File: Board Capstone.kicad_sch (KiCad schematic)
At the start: 14 parts, among them J101 Power, J102 Conn_JetsonNano, J103 Status_LED, J104 Warning_LED, J105 Lidar Power, SW101 SW_Pairing, U101 SN74LV1T125DBV, U102 SN74LV1T125DBV

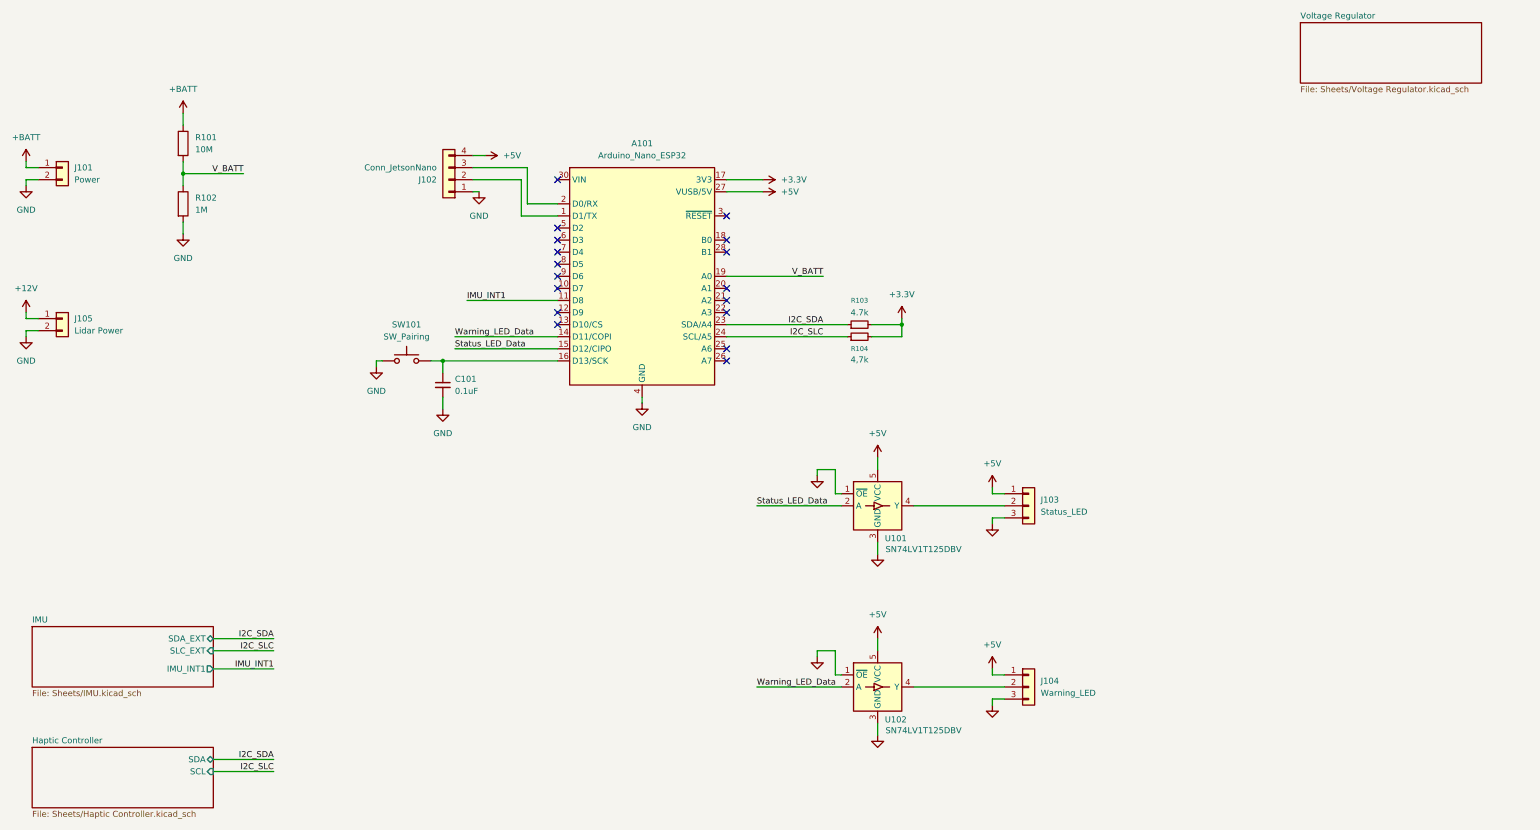
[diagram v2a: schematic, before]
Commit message: Rev 2.0 Remove MCU, IMU, Haptics controller. Add Jetson connector, Battery protection, ADC. Etc.
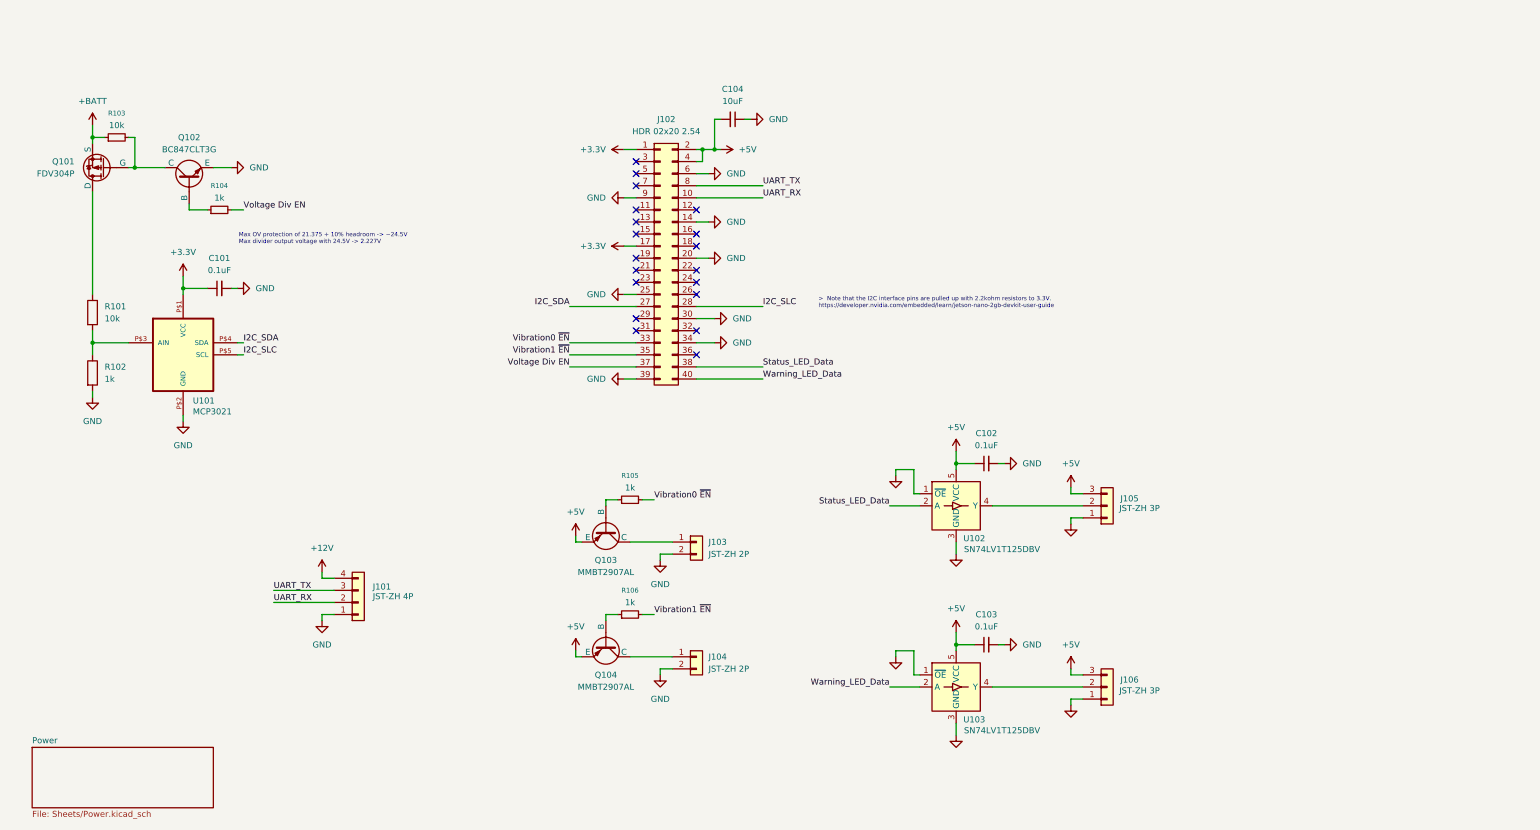
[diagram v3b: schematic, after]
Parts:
- removed A101: Arduino_Nano_ESP32, Module:Arduino_Nano, symbol MCU_Module:Arduino_Nano_ESP32
- removed J101: Power, Connector_JST:JST_XH_B2B-XH-A_1x02_P2.50mm_Vertical, symbol Connector_Generic:Conn_01x02
- removed J102: Conn_JetsonNano, Connector_JST:JST_XH_B4B-XH-A_1x04_P2.50mm_Vertical, symbol Connector_Generic:Conn_01x04
- removed J105: Lidar Power, Connector_JST:JST_XH_B2B-XH-A_1x02_P2.50mm_Vertical, symbol Connector_Generic:Conn_01x02
- removed SW101: SW_Pairing, Button_Switch_THT:SW_PUSH_6mm, symbol Switch:SW_Push
- added C102, C103: 0.1uF, Capacitor_SMD:C_1206_3216Metric_Pad1.33x1.80mm_HandSolder, symbol Device:C_Small
- added C104: 10uF, Capacitor_SMD:C_1206_3216Metric_Pad1.33x1.80mm_HandSolder, symbol Device:C_Small
- added J101: JST-ZH 4P, Connector_JST:JST_ZH_B4B-ZR_1x04_P1.50mm_Vertical, symbol Connector_Generic:Conn_01x04
- added J102: HDR 02x20 2.54, Connector_IDC:IDC-Header_2x20_P2.54mm_Horizontal, symbol Connector_Generic:Conn_02x20_Odd_Even
- added J103, J104: JST-ZH 2P, Connector_JST:JST_ZH_B2B-ZR_1x02_P1.50mm_Vertical, symbol Connector_Generic:Conn_01x02
- added Q101: FDV304P, Package_TO_SOT_SMD:SOT-23-3, symbol Simulation_SPICE:PMOS
- added Q102: BC847CLT3G, Package_TO_SOT_SMD:SOT-23, symbol Simulation_SPICE:NPN
- added Q103, Q104: MMBT2907AL, Package_TO_SOT_SMD:SOT-23, symbol Simulation_SPICE:PNP
- added R105, R106: 1k, Resistor_SMD:R_1206_3216Metric_Pad1.30x1.75mm_HandSolder, symbol Device:R_Small
- added U101: MCP3021, MCP3021:SOT-23, symbol MCP3021:MCP3021
- J105: renamed from J103; value Status_LED -> JST-ZH 3P; footprint Connector_JST:JST_ZH_B3B-ZR_1x03_P1.50mm_Vertical -> Connector_JST:JST_ZH_B2B-ZR_1x02_P1.50mm_Vertical
- J106: renamed from J104; value Warning_LED -> JST-ZH 3P
- R101: value 10M -> 10k; footprint Resistor_THT:R_Axial_DIN0207_L6.3mm_D2.5mm_P7.62mm_Horizontal -> Resistor_SMD:R_1206_3216Metric_Pad1.30x1.75mm_HandSolder
- R102: value 1M -> 1k; footprint Resistor_THT:R_Axial_DIN0207_L6.3mm_D2.5mm_P7.62mm_Horizontal -> Resistor_SMD:R_1206_3216Metric_Pad1.30x1.75mm_HandSolder
- R103: value 4.7k -> 10k
- R104: value 4,7k -> 1k
- renumbered U101 to U102, U102 to U103
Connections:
- net +12V: now also J101.4 (Pin_4)
- net +3.3V: now also C101.1, J102.1 (Pin_1), J102.17 (Pin_17), U101.P$1 (VCC); no longer R103.2, R104.2
- net +5V: now also J105.3 (Pin_3), J106.3 (Pin_3), C102.1, C103.1, C104.2, J102.2 (Pin_2), J102.4 (Pin_4), Q103.3 (E), Q104.3 (E); no longer J105.1 (Pin_1), J106.1 (Pin_1)
- net +BATT: now also R103.1, Q101.3 (S); no longer R101.1
- net GND: now also J105.1 (Pin_1), J106.1 (Pin_1), C102.2, C103.2, C104.1, J101.1 (Pin_1), J102.14 (Pin_14), J102.20 (Pin_20), J102.25 (Pin_25), J102.30 (Pin_30), J102.34 (Pin_34), J102.39 (Pin_39), J102.6 (Pin_6), J102.9 (Pin_9), J103.2 (Pin_2), J104.2 (Pin_2), Q102.3 (E), U101.P$2 (GND); no longer J105.3 (Pin_3), J106.3 (Pin_3)
- net I2C_SDA: now also J102.27 (Pin_27), U101.P$4 (SDA); no longer R103.1
- net I2C_SLC: now also J102.28 (Pin_28), U101.P$5 (SCL); no longer R104.1
- net Status_LED_Data: now also J102.38 (Pin_38)
- net Warning_LED_Data: now also J102.40 (Pin_40)
- net V_BATT: no longer names the net of R101.2, R102.1
- net V_BATT: now also U101.P$3 (AIN)
- new net: Q101.1 (D), R101.1
- new net: Q101.2 (G), Q102.1 (C), R103.2
- new net: Q104.2 (B), R106.1
- new net: J103.1 (Pin_1), Q103.1 (C)
- new net: Q103.2 (B), R105.1
- new net: Q102.2 (B), R104.1
- new net: J104.1 (Pin_1), Q104.1 (C)
- new net UART_RX: J101.2 (Pin_2), J102.10 (Pin_10)
- new net UART_TX: J101.3 (Pin_3), J102.8 (Pin_8)
- new net Vibration0 ~{EN}: J102.33 (Pin_33), R105.2
- new net Vibration1 ~{EN}: J102.35 (Pin_35), R106.2
- new net Voltage Div EN: J102.37 (Pin_37), R104.2
- no-connect marks 17 -> 19
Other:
- sheet Voltage Regulator renamed Power
- removed sheet Haptic Controller
- removed sheet IMU
- sheet Power: file Sheets/Voltage Regulator.kicad_sch -> Sheets/Power.kicad_sch
- note added: "> Note that the I2C interface pins are pulled up with 2.2kohm resistors to 3.3V. https://developer.nvidia.com/embedded/learn/jetson-nano-2gb-devkit-user-guide"
- note added: "Max OV protection of 21.375 + 10% headroom -> ~24.5V Max divider output voltage with 24.5V -> 2.227V"
- moved on the sheet: J105, J106, R101, R102, U102, U103

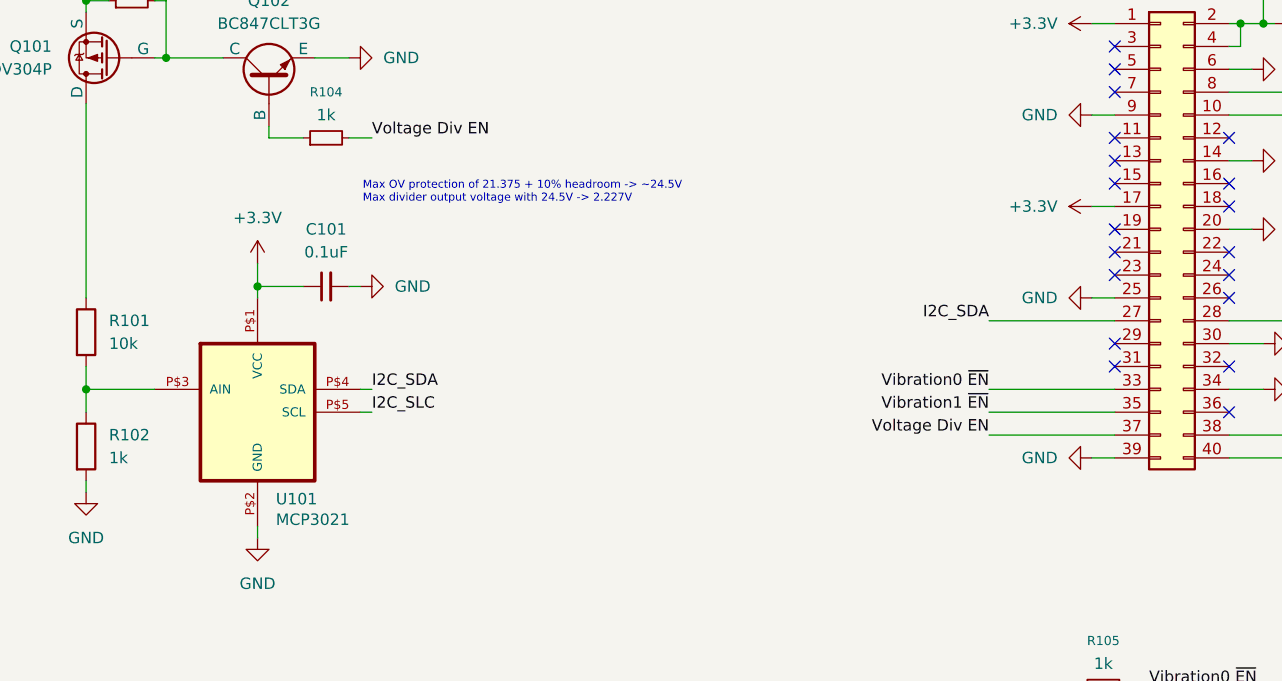
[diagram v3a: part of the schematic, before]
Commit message: Rev 2.1 Add pcb and footprint changes
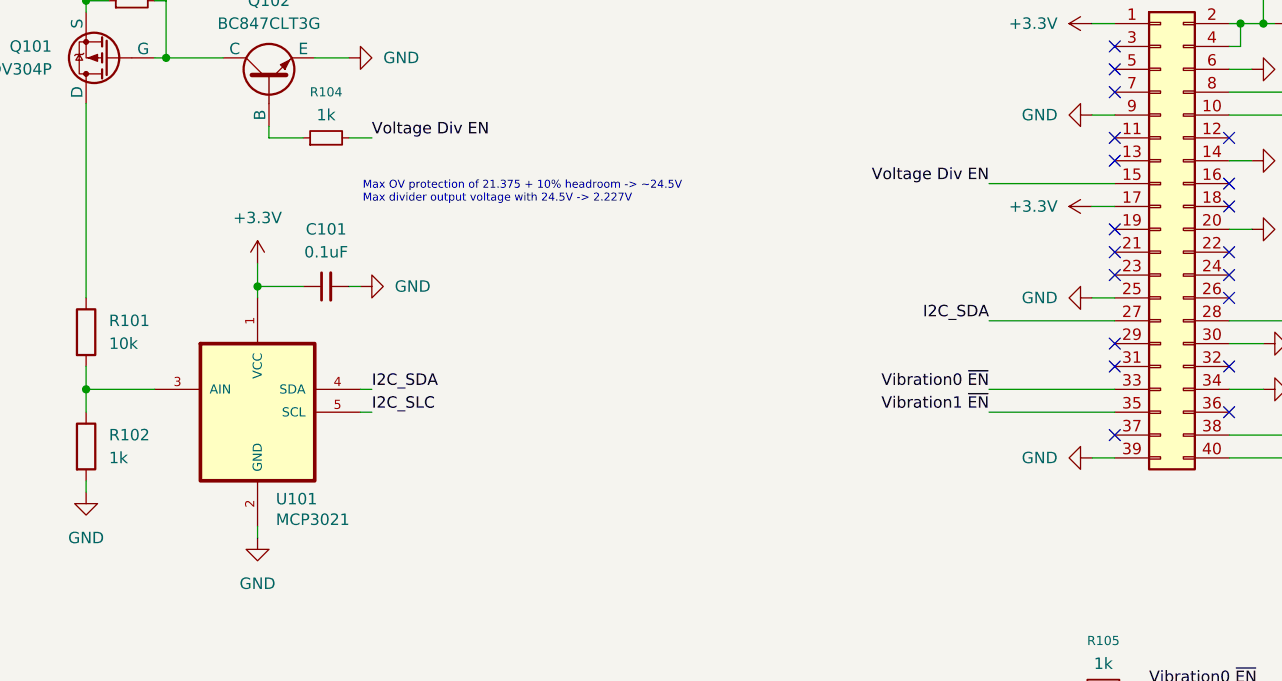
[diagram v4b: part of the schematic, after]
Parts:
- J101: footprint Connector_JST:JST_ZH_B4B-ZR_1x04_P1.50mm_Vertical -> Connector_JST:JST_ZH_S4B-ZR-SM4A-TF_1x04-1MP_P1.50mm_Horizontal
- J103, J104: footprint Connector_JST:JST_ZH_B2B-ZR_1x02_P1.50mm_Vertical -> Connector_JST:JST_ZH_S2B-ZR-SM4A-TF_1x02-1MP_P1.50mm_Horizontal
- J105: footprint Connector_JST:JST_ZH_B2B-ZR_1x02_P1.50mm_Vertical -> Connector_JST:JST_ZH_S3B-ZR-SM4A-TF_1x03-1MP_P1.50mm_Horizontal
- J106: footprint Connector_JST:JST_ZH_B3B-ZR_1x03_P1.50mm_Vertical -> Connector_JST:JST_ZH_S3B-ZR-SM4A-TF_1x03-1MP_P1.50mm_Horizontal
- U101: footprint MCP3021:SOT-23 -> Package_TO_SOT_SMD:SOT-23-5_HandSoldering
- U102, U103: footprint Package_TO_SOT_SMD:SOT-23-5 -> Package_TO_SOT_SMD:SOT-23-5_HandSoldering
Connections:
- net +3.3V: now also U101.1 (VCC); no longer U101.P$1 (VCC)
- net GND: now also U101.2 (GND); no longer U101.P$2 (GND)
- net I2C_SDA: now also U101.4 (SDA); no longer U101.P$4 (SDA)
- net I2C_SLC: now also U101.5 (SCL); no longer U101.P$5 (SCL)
- net Voltage Div EN: now also J102.15 (Pin_15); no longer J102.37 (Pin_37)
- net at R101.2, R102.1: now also U101.3 (AIN); no longer U101.P$3 (AIN)
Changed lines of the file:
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@@
 	(title_block
 		(title "Cyclops (Team 30)")
-		(date "2025-12-10")
-		(rev "2.0")
+		(date "2025-12-16")
+		(rev "2.1")
 		(company "Concordia University, Department of Electrical and Computer Engineering")
 	)
@@
 	)
 	(junction
-		(at 168.91 39.37)
+		(at 38.1 80.01)
 		(diameter 0)
 		(color 0 0 0 0)
 	)
 	(junction
-		(at 38.1 80.01)
+		(at 168.91 39.37)
 		(diameter 0)
 		(color 0 0 0 0)
@@
 	)
 	(no_connect
-		(at 152.4 57.15)
-	)
-	(no_connect
 		(at 165.1 64.77)
 	)
@@
 		(at 152.4 62.23)
 	)
+	(no_connect
+		(at 152.4 85.09)
+	)
 	(wire
 		(pts
@@
 	(wire
 		(pts
-			(xy 38.1 80.01) (xy 38.1 82.55)
-		)
-		(stroke
-			(width 0)
-			(type default)
-		)
-	)
-	(wire
-		(pts
 			(xy 138.43 72.39) (xy 152.4 72.39)
 		)
@@
 	(wire
 		(pts
+			(xy 38.1 80.01) (xy 45.72 80.01)
+		)
+		(stroke
+			(width 0)
+			(type default)
+		)
+	)
+	(wire
+		(pts
 			(xy 46.99 43.18) (xy 53.34 43.18)
 		)
@@
 	(wire
 		(pts
+			(xy 138.43 57.15) (xy 152.4 57.15)
+		)
+		(stroke
+			(width 0)
+			(type default)
+		)
+	)
+	(wire
+		(pts
 			(xy 210.82 106.68) (xy 207.01 106.68)
 		)
@@
 	(wire
 		(pts
-			(xy 138.43 85.09) (xy 152.4 85.09)
-		)
-		(stroke
-			(width 0)
-			(type default)
-		)
-	)
-	(wire
-		(pts
 			(xy 157.48 148.59) (xy 160.02 148.59)
 		)
@@
 	(wire
 		(pts
-			(xy 38.1 80.01) (xy 45.72 80.01)
+			(xy 38.1 80.01) (xy 38.1 82.55)
 		)
 		(stroke
@@
 		)
 	)
-	(label "Voltage Div EN"
-		(at 138.43 85.09 180)
+	(label "I2C_SDA"
+		(at 138.43 72.39 180)
 		(effects
 			(font
@@
 		)
 	)
-	(label "I2C_SDA"
-		(at 138.43 72.39 180)
+	(label "Voltage Div EN"
+		(at 138.43 57.15 180)
 		(effects
 			(font
@@
 			)
 		)
-		(property "Footprint" "Connector_JST:JST_ZH_B2B-ZR_1x02_P1.50mm_Vertical"
+		(property "Footprint" "Connector_JST:JST_ZH_S3B-ZR-SM4A-TF_1x03-1MP_P1.50mm_Horizontal"
 			(at 251.46 114.3 0)
 			(effects
@@
 			)
 		)
-		(property "Footprint" "Connector_JST:JST_ZH_B2B-ZR_1x02_P1.50mm_Vertical"
+		(property "Footprint" "Connector_JST:JST_ZH_S2B-ZR-SM4A-TF_1x02-1MP_P1.50mm_Horizontal"
 			(at 165.1 121.92 0)
 			(effects
@@
 			)
 		)
-		(property "Footprint" "Connector_JST:JST_ZH_B3B-ZR_1x03_P1.50mm_Vertical"
+		(property "Footprint" "Connector_JST:JST_ZH_S3B-ZR-SM4A-TF_1x03-1MP_P1.50mm_Horizontal"
 			(at 251.46 152.4 0)
 			(effects
@@
 			)
 		)
-		(property "Footprint" "Package_TO_SOT_SMD:SOT-23-5"
+		(property "Footprint" "Package_TO_SOT_SMD:SOT-23-5_HandSoldering"
 			(at 219.71 138.43 0)
 			(effects
@@
 			)
 		)
-		(property "Footprint" "Connector_JST:JST_ZH_B4B-ZR_1x04_P1.50mm_Vertical"
+		(property "Footprint" "Connector_JST:JST_ZH_S4B-ZR-SM4A-TF_1x04-1MP_P1.50mm_Horizontal"
 			(at 93.98 134.62 0)
 			(effects
@@
 			)
 		)
-		(property "Footprint" "Package_TO_SOT_SMD:SOT-23-5"
+		(property "Footprint" "Package_TO_SOT_SMD:SOT-23-5_HandSoldering"
 			(at 219.71 176.53 0)
 			(effects
@@
 			)
 		)
-		(property "Footprint" "Connector_JST:JST_ZH_B2B-ZR_1x02_P1.50mm_Vertical"
+		(property "Footprint" "Connector_JST:JST_ZH_S2B-ZR-SM4A-TF_1x02-1MP_P1.50mm_Horizontal"
 			(at 165.1 146.05 0)
 			(effects
@@
 			)
 		)
-		(property "Footprint" "MCP3021:SOT-23"
+		(property "Footprint" "Package_TO_SOT_SMD:SOT-23-5_HandSoldering"
 			(at 63.5 88.9 0)
 			(effects
@@
 			)
 		)
-		(pin "P$3"
+		(pin "3"
 		)
-		(pin "P$4"
+		(pin "4"
 		)
-		(pin "P$1"
+		(pin "5"
 		)
-		(pin "P$5"
+		(pin "2"
 		)
-		(pin "P$2"
+		(pin "1"
 		)
 		(instances

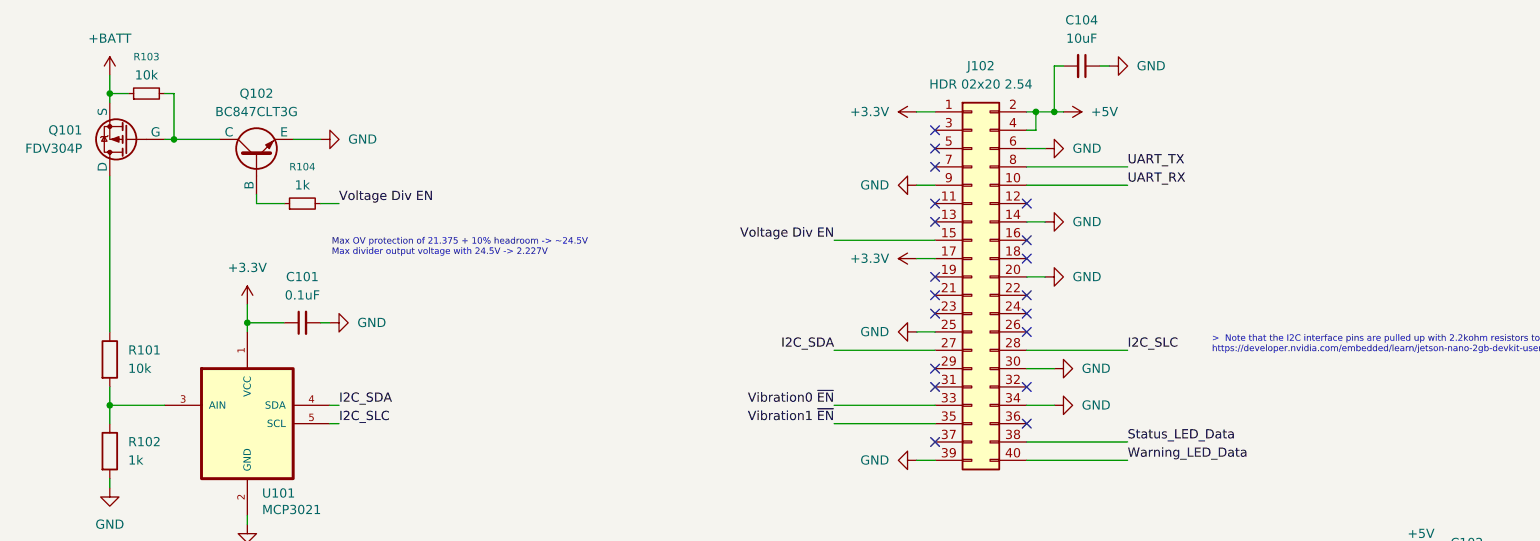
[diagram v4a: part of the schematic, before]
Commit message: Rev 2.2 Added test point and status LED
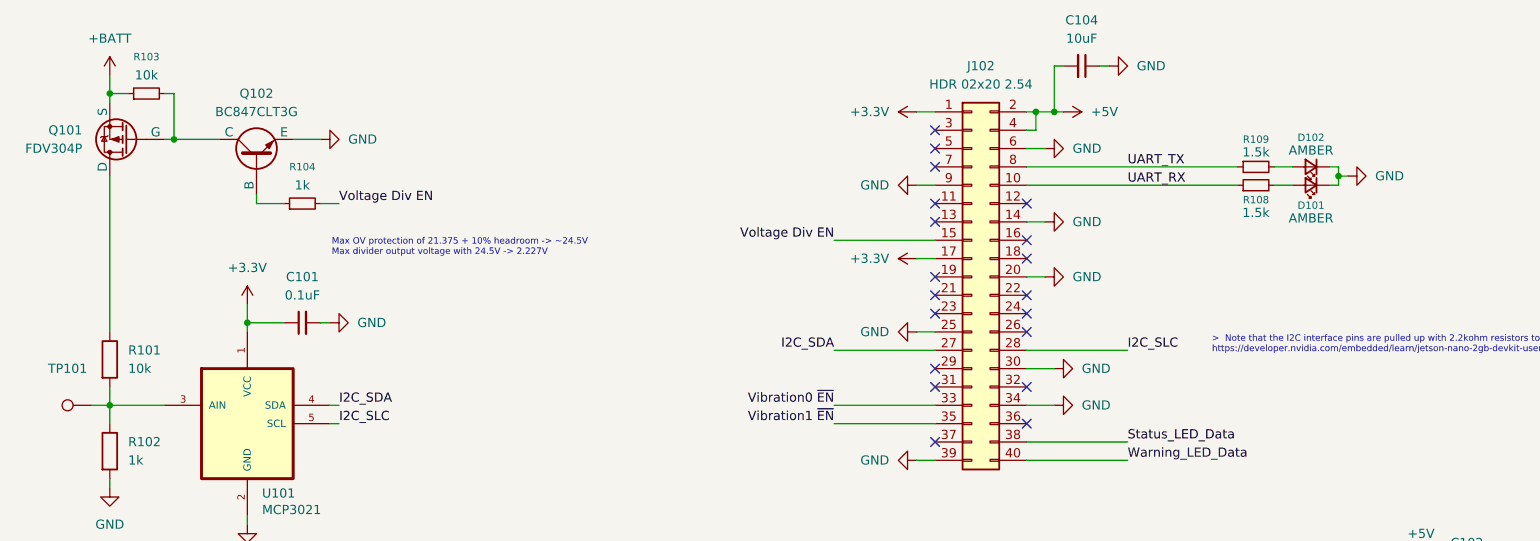
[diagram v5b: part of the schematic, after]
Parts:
- added D101, D102: AMBER, LED_SMD:LED_0603_1608Metric_Pad1.05x0.95mm_HandSolder, symbol Device:LED_Small
- added R108, R109: 1.5k, Resistor_SMD:R_1206_3216Metric_Pad1.30x1.75mm_HandSolder, symbol Device:R_Small
- added TP101: ~, TestPoint:TestPoint_Pad_D2.5mm, symbol Connector:TestPoint
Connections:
- net GND: now also D101.1 (K), D102.1 (K)
- net UART_RX: now also R108.1
- net UART_TX: now also R109.1
- net at R101.2, R102.1, U101.3 (AIN): now also TP101.1
- new net: D101.2 (A), R108.2
- new net: D102.2 (A), R109.2
